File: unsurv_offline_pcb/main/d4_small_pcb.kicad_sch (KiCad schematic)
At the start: 54 parts, among them J1 U_FL-R-SMT-1_10_, J2 S2B-PH-SM4-TB_LF__SN_, Q1 UMH3N, Q2 Q_PMOS_GSD, U1 TTGO-Micro32-ESP32, U2 MCP73831-2-OT, U3 CAM-M8C-0-10, U4 AP2112K-3.3, U5 CH340G, U6 RF430CL330H, U7 BMA400-I2C, U8 RFM95W-868S2

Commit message: v 0.3.1 PCB
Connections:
- net 13: now also U8.14 (DIO0); no longer U6.8 (INT0)
- net 32: now also U6.8 (INT0); no longer U8.14 (DIO0)

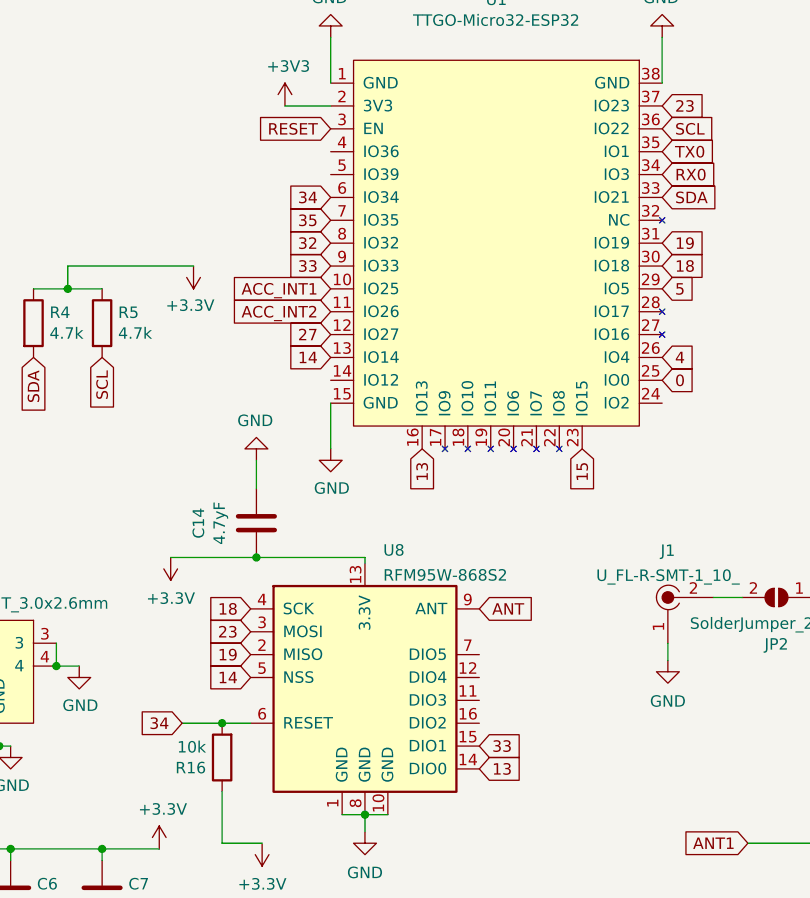
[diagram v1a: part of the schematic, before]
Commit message: added new 3D case + PCB rework
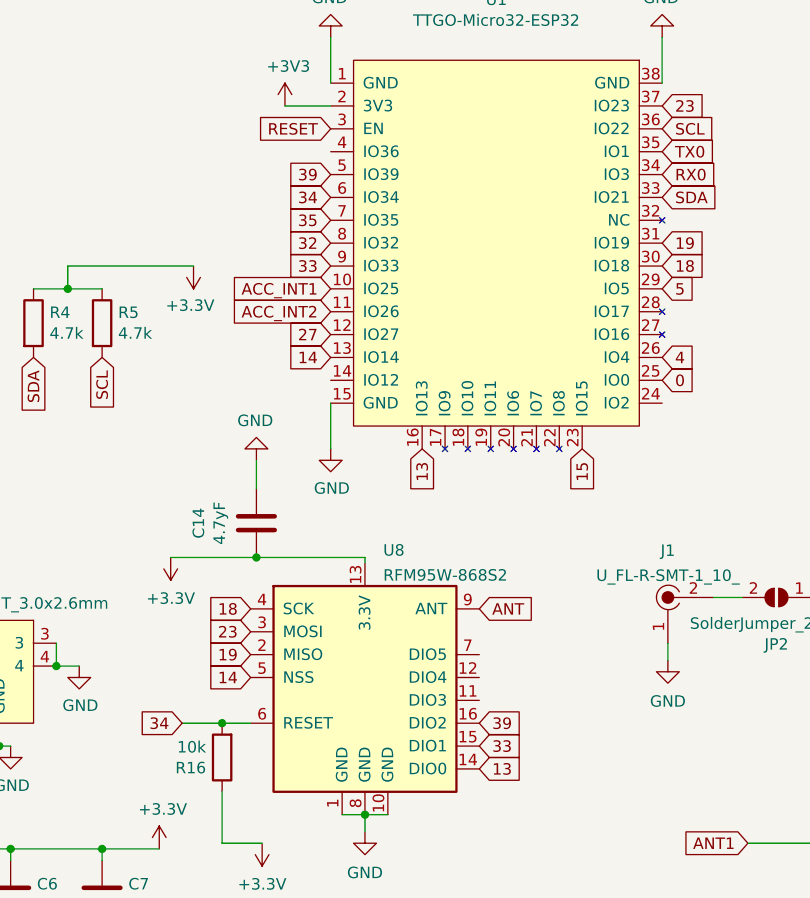
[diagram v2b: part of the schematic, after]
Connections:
- net 39: now reaches U1.5 (IO39)
- net 39: now also U8.16 (DIO2)

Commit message: pre rework
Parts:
- removed D4: D_Schottky, Diode_SMD:D_SOD-323, symbol Device:D_Schottky
- removed Q2: Q_PMOS_GSD, Package_TO_SOT_SMD:SOT-23, symbol Device:Q_PMOS_GSD
- removed R11: 100k, Resistor_SMD:R_0603_1608Metric, symbol Device:R
- removed U2: MCP73831-2-OT, Package_TO_SOT_SMD:SOT-23-5, symbol Battery_Management:MCP73831-2-OT
- added C15: 1yF, Capacitor_SMD:C_0603_1608Metric, symbol Device:C
- added U9: PQ2581DLHT, unsurv_offline_pcb_footprints:BQ2581DLHT, symbol unsurv_offline_pcb_symbols:PQ2581DLHT
- C1: value 4.7yF -> 10yF
- C2: value 4.7yF -> 1yF
- R2: value 10k -> 1k
- R3: value 1k -> 10k
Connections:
- net +5V: now also C15.2, U9.10 (IN); no longer C2.2
- net +BATT: now also C2.2, U9.2 (BAT); no longer C1.2
- net 35: now also R7.1, R8.2; no longer R7.2, R8.1
- net GND: now also C1.2, R3.2, R7.2, C15.1, U9.11 (PAD), U9.5 (GND); no longer C1.1, R2.2, R8.2
- net SCL: now also U9.8 (SCL)
- net SDA: now also U9.7 (SDA)
- net at R3.1: now also U9.6 (TS/MR)
- net at R2.1: now also U9.3 (/PG_GPO)
- net at D3.1 (K): now also R2.2; no longer R3.2
- net VCC: now reaches C8.2, R10.2, U4.1 (VIN)
- net VCC: now also C1.1, U9.1 (SYS)
- net at JP1.2 (B): now also R8.1; no longer R7.1
- net 36: now reaches U1.4 (IO36)
- net 36: now also U9.9 (/INT)
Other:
- moved on the sheet: C8, J2, R4, R5
